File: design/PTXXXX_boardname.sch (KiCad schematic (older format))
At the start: 0 parts

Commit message: place some dummy parts for 1.0 1A release
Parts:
- added U?: IR4302, Package_DFN_QFN:Infineon_PQFN-44-31-5EP_7x7mm_P0.5mm, symbol Amplifier_Audio:IR4302
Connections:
- new net: U?.15 (COM), U?.28 (COM), U?.31 (COM)
- new net: U?.18 (VS1), U?.20 (VS1)
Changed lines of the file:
@@
 Comment4 ""
 $EndDescr
+$Comp
+L Amplifier_Audio:IR4302 U?
+U 1 1 5E3D5177
+P 4650 3250
+F 0 "U?" H 4650 4231 50  0000 C CNN
+F 1 "IR4302" H 4650 4140 50  0000 C CNN
+F 2 "Package_DFN_QFN:Infineon_PQFN-44-31-5EP_7x7mm_P0.5mm" H 4650 3250 50  0001 C CIN
+F 3 "https://www.infineon.com/dgdl/ir4302.pdf?fileId=5546d462533600a4015355d602a9181d" H 4650 3250 50  0001 C CNN
+	1    4650 3250
+	1    0    0    -1
+$EndComp
 $EndSCHEMATC

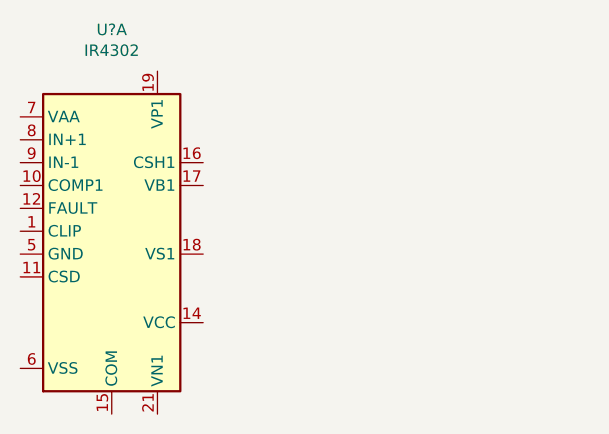
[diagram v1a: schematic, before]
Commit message: added R1 1k resistor, and annotated IC as U1
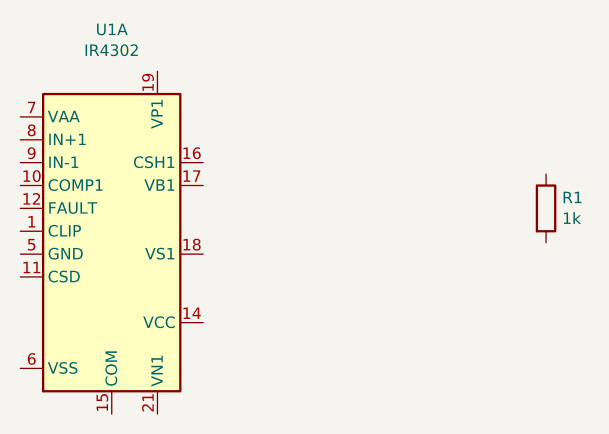
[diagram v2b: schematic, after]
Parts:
- added R1: 1k, Resistor_SMD:R_0805_2012Metric, symbol Device:R
- gave numbers to parts that had none: 1
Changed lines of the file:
@@
 $EndDescr
 $Comp
-L Amplifier_Audio:IR4302 U?
+L Amplifier_Audio:IR4302 U1
 U 1 1 5E3D5177
 P 4650 3250
-F 0 "U?" H 4650 4231 50  0000 C CNN
+F 0 "U1" H 4650 4231 50  0000 C CNN
 F 1 "IR4302" H 4650 4140 50  0000 C CNN
 F 2 "Package_DFN_QFN:Infineon_PQFN-44-31-5EP_7x7mm_P0.5mm" H 4650 3250 50  0001 C CIN
@@
 	1    0    0    -1
 $EndComp
+$Comp
+L Device:R R1
+U 1 1 5E3D59F6
+P 6550 3050
+F 0 "R1" H 6620 3096 50  0000 L CNN
+F 1 "1k" H 6620 3005 50  0000 L CNN
+F 2 "Resistor_SMD:R_0805_2012Metric" V 6480 3050 50  0001 C CNN
+F 3 "~" H 6550 3050 50  0001 C CNN
+	1    6550 3050
+	1    0    0    -1
+$EndComp
